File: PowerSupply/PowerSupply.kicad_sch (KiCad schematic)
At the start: 29 parts, among them IC1 MCP73832T-2DCI_OT, J1 Conn_01x04_Male, J2 Barrel_Jack, Q1 DMP2045U-7, Q2 DMP2045U-7, U1 AP3012, U2 AP3012

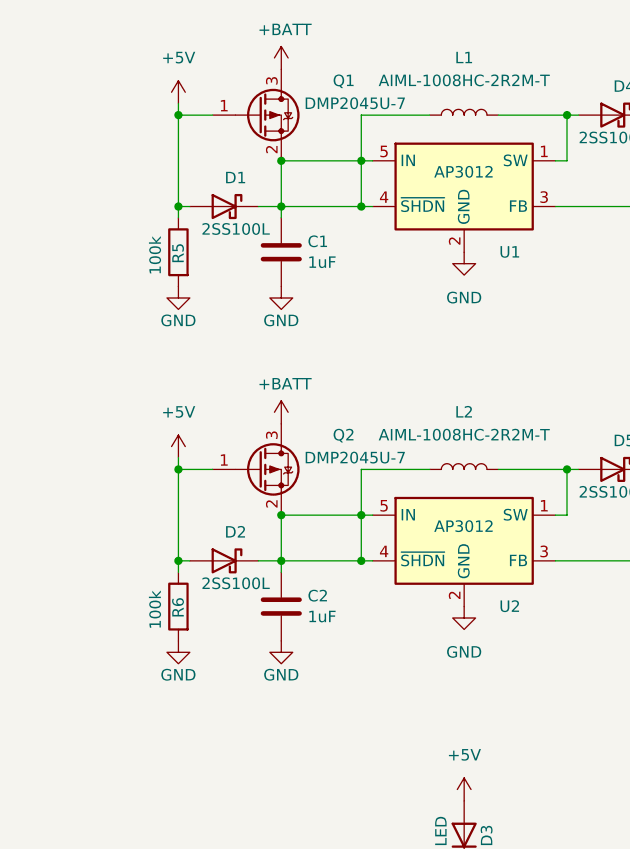
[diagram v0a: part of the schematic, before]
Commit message: Added power switch
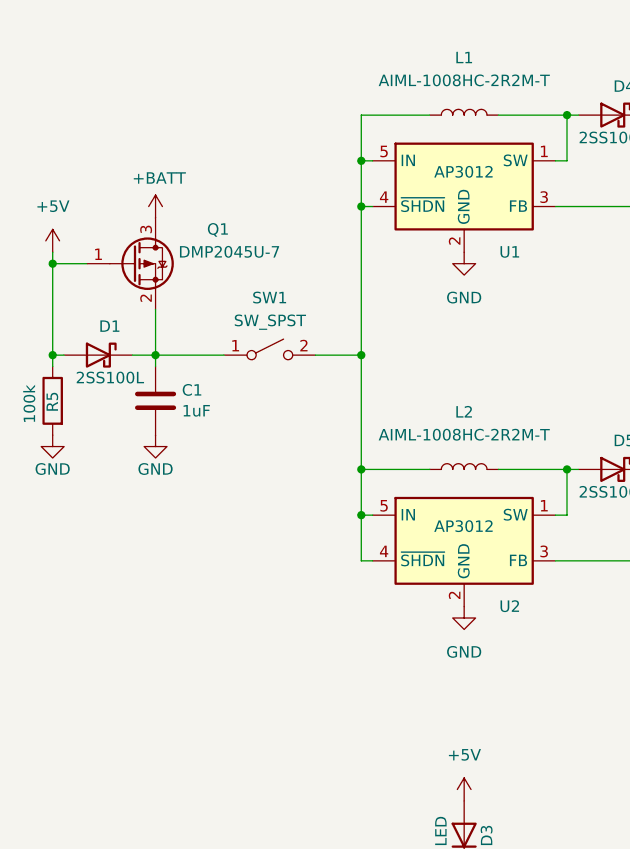
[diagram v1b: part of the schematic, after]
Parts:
- removed C2: 1uF, Capacitor_SMD:C_0603_1608Metric, symbol Device:C
- removed D2: 2SS100L, Diode_SMD:D_SOD-123F, symbol Device:D_Schottky
- removed Q2: DMP2045U-7, Package_TO_SOT_SMD:SOT-23, symbol Transistor_FET:DMG2301L
- removed R6: 100k, Resistor_SMD:R_0603_1608Metric, symbol Device:R
- added SW1: SW_SPST, Connector_PinHeader_2.54mm:PinHeader_1x02_P2.54mm_Horizontal, symbol Switch:SW_SPST
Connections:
- net at C1.1, D1.1 (K), Q1.2 (S): now also SW1.1 (A); no longer L1.1, U1.4 (~{SHDN}), U1.5 (IN)
- net at L2.1, U2.4 (~{SHDN}), U2.5 (IN): now also L1.1, U1.4 (~{SHDN}), U1.5 (IN), SW1.2 (B)
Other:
- moved on the sheet: C1, D1, Q1, R5

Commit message: Moved capacitors for regulators to other side of power switch.
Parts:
- added C2: 1uF, Capacitor_SMD:C_0603_1608Metric, symbol Device:C
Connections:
- net GND: now also C2.2
- net at D1.1 (K), Q1.2 (S), SW1.1 (A): no longer C1.1
- net at L1.1, L2.1, SW1.2 (B)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: now also C1.1, C2.1
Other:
- moved on the sheet: C1, D1, Q1, R5, SW1

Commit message: Added silk screen and fabrication files.
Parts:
- D1, D4, D5: value 2SS100L -> NRVB120VLSFT1G
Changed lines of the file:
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@@
-    (stroke (width 0) (type default) (color 0 0 0 0))
-  )
-  (wire (pts (xy 59.69 59.69) (xy 59.69 60.96))
     (stroke (width 0) (type default) (color 0 0 0 0))
   )
@@
   )
   (symbol (lib_id "Device:L") (at 99.06 72.39 90) (unit 1)
-    (in_bom yes) (on_board yes) (fields_autoplaced)
-    (property "Reference" "L2" (id 0) (at 99.06 66.04 90))
-    (property "Value" "AIML-1008HC-2R2M-T" (id 1) (at 99.06 68.58 90))
+    (in_bom yes) (on_board yes)
+    (property "Reference" "L2" (id 0) (at 99.06 69.85 90))
+    (property "Value" "AIML-1008HC-2R2M-T" (id 1) (at 99.695 67.31 90))
     (property "Footprint" "Inductor_SMD:L_1008_2520Metric" (id 2) (at 99.06 72.39 0)
       (effects (font (size 1.27 1.27)) hide)
@@
   (symbol (lib_id "Device:D_Schottky") (at 115.57 33.02 0) (mirror y) (unit 1)
     (in_bom yes) (on_board yes)
-    (property "Reference" "D4" (id 0) (at 116.84 29.845 0))
-    (property "Value" "2SS100L" (id 1) (at 115.57 35.56 0))
+    (property "Reference" "D4" (id 0) (at 115.57 36.195 0))
+    (property "Value" "NRVB120VLSFT1G" (id 1) (at 116.84 30.48 0))
     (property "Footprint" "Diode_SMD:D_SOD-123F" (id 2) (at 115.57 33.02 0)
       (effects (font (size 1.27 1.27)) hide)
@@
   )
   (symbol (lib_id "Device:L") (at 99.06 33.02 90) (unit 1)
-    (in_bom yes) (on_board yes) (fields_autoplaced)
-    (property "Reference" "L1" (id 0) (at 99.06 26.67 90))
-    (property "Value" "AIML-1008HC-2R2M-T" (id 1) (at 99.06 29.21 90))
+    (in_bom yes) (on_board yes)
+    (property "Reference" "L1" (id 0) (at 99.06 30.48 90))
+    (property "Value" "AIML-1008HC-2R2M-T" (id 1) (at 99.06 27.94 90))
     (property "Footprint" "Inductor_SMD:L_1008_2520Metric" (id 2) (at 99.06 33.02 0)
       (effects (font (size 1.27 1.27)) hide)
@@
   (symbol (lib_id "Device:D_Schottky") (at 115.57 72.39 0) (mirror y) (unit 1)
     (in_bom yes) (on_board yes)
-    (property "Reference" "D5" (id 0) (at 116.84 69.215 0))
-    (property "Value" "2SS100L" (id 1) (at 115.57 74.93 0))
+    (property "Reference" "D5" (id 0) (at 115.57 75.565 0))
+    (property "Value" "NRVB120VLSFT1G" (id 1) (at 115.57 69.85 0))
     (property "Footprint" "Diode_SMD:D_SOD-123F" (id 2) (at 115.57 72.39 0)
       (effects (font (size 1.27 1.27)) hide)
@@
   (symbol (lib_id "Device:D_Schottky") (at 53.34 59.69 0) (mirror y) (unit 1)
     (in_bom yes) (on_board yes)
-    (property "Reference" "D1" (id 0) (at 54.61 56.515 0))
-    (property "Value" "2SS100L" (id 1) (at 54.61 62.23 0))
+    (property "Reference" "D1" (id 0) (at 53.34 62.865 0))
+    (property "Value" "NRVB120VLSFT1G" (id 1) (at 50.8 56.515 0))
     (property "Footprint" "Diode_SMD:D_SOD-123F" (id 2) (at 53.34 59.69 0)
       (effects (font (size 1.27 1.27)) hide)
@@
     )
     (path "/d0fa12a7-f6a9-47df-94c0-7e0d21d2fc9c"
-      (reference "D1") (unit 1) (value "2SS100L") (footprint "Diode_SMD:D_SOD-123F")
+      (reference "D1") (unit 1) (value "NRVB120VLSFT1G") (footprint "Diode_SMD:D_SOD-123F")
     )
     (path "/c2ef9bcd-6dac-4a06-94a7-eed2e9d97ccf"
@@
     )
     (path "/9089088a-9e65-48e6-9fdb-8bd937ca71a4"
-      (reference "D4") (unit 1) (value "2SS100L") (footprint "Diode_SMD:D_SOD-123F")
+      (reference "D4") (unit 1) (value "NRVB120VLSFT1G") (footprint "Diode_SMD:D_SOD-123F")
     )
     (path "/aef2a9a2-02ce-430c-809a-7dc9d58d317e"
-      (reference "D5") (unit 1) (value "2SS100L") (footprint "Diode_SMD:D_SOD-123F")
+      (reference "D5") (unit 1) (value "NRVB120VLSFT1G") (footprint "Diode_SMD:D_SOD-123F")
     )
     (path "/b79a028e-e2d4-44dd-80c3-e7486cd34dfe"

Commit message: Optimized board and changed a few component part numbers based on availability. This version was first production board ordered.
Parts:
- removed C2: 1uF, Capacitor_SMD:C_0603_1608Metric, symbol Device:C
- added LOGO1: Logo_Open_Hardware_Small, Library:TUNL LOGO small, symbol Graphic:Logo_Open_Hardware_Small
- added R6: 470, Resistor_SMD:R_0603_1608Metric, symbol Device:R
- D1, D4, D5: value NRVB120VLSFT1G -> MBR1020VL_R1_00001
- IC1: value MCP73832T-2DCI_OT -> MCP73832T-2DCI/OT
- J2: value Barrel_Jack -> PJ-002A
- SW1: value SW_SPST -> RP3508BBLKGRNGRNNS; footprint Connector_PinHeader_2.54mm:PinHeader_1x02_P2.54mm_Horizontal -> Library:RP3508x; symbol Switch:SW_SPST -> Switch:SW_Push_LED
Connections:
- net GND: now also R6.1
- net VBUS: now reaches C1.1, L1.1, L2.1, SW1.2, U1.4 (~{SHDN}), U1.5 (IN), U2.4 (~{SHDN}), U2.5 (IN)
- net VBUS: now also SW1.4 (A)
- new net: R6.2, SW1.3 (K)
